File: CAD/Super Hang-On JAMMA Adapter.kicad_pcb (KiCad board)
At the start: 2 copper layers, 111 x 80.2 mm, 30 parts, among them U1 LM386, U2 MCP4902, U3 ATMEGA328

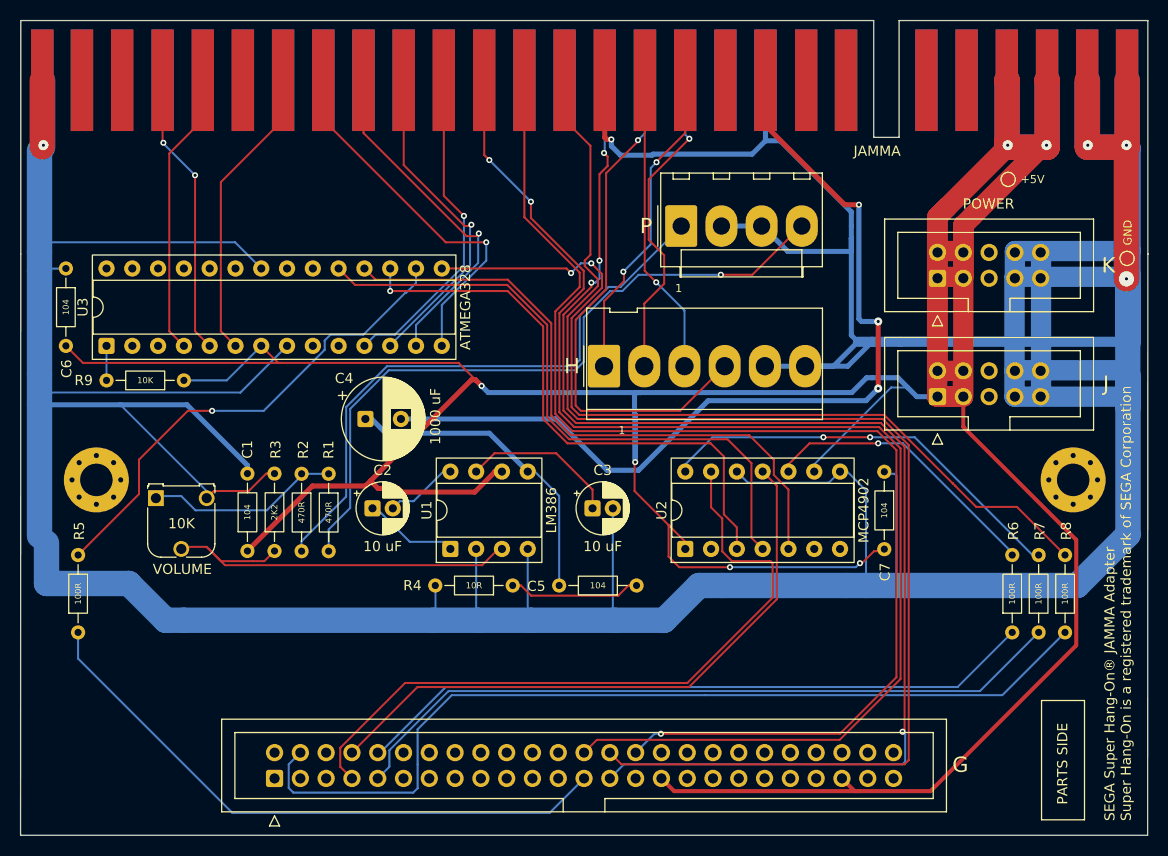
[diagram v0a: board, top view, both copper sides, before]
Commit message: Adjust positioning of 50-pin, move text to bottom, slight tweaks
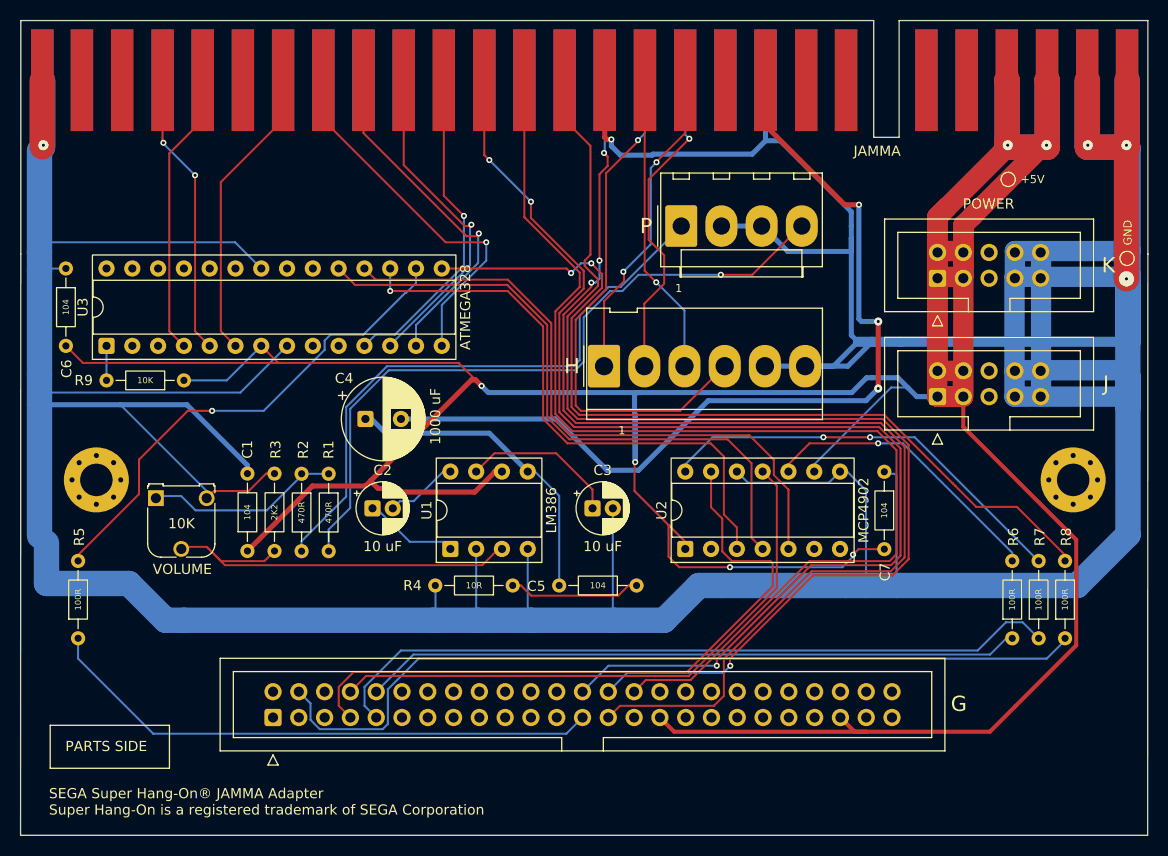
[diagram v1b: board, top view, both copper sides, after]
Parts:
- moved G 6.00 mm to (118.8, 132.0)
- moved R5 0.58 mm to (99.6, 124.2)
- moved R6 0.58 mm to (191.6, 124.2)
- moved R7 0.58 mm to (194.2, 124.2)
- moved R8 0.58 mm to (196.8, 124.2)
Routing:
- net TEST: track 131.6 -> 117.2 mm, vias 0 -> 1
- net SERVICE: track 130.8 -> 118.6 mm, vias 4 -> 3
- net COIN_1: track 122.3 -> 112.9 mm, vias 1 -> 0
- net 1P_START: track 129.7 -> 120.6 mm, vias 2 -> 3
- net BRK: track 90.5 -> 83.8 mm
- net TURBO: track 60.1 -> 55.4 mm
- net REFA: track 69.4 -> 66.4 mm
- net REFB: track 61.3 -> 58.3 mm
- net STEER: track 67.4 -> 64.8 mm
- net +5V: track 413.1 -> 411.8 mm
- net ACCEL: track 72.0 -> 73.2 mm
- net VOUTB: track 28.3 -> 28.9 mm
- net PB2: track 48.5 -> 49.1 mm
- net PB1: track 85.8 -> 86.4 mm
